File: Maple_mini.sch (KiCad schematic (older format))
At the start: 24 parts, among them P1 CONN_01X03, Q1 Q_NPN_BEC, Q2 Q_NPN_BEC, SW1 SW_PUSH, SW2 SW_PUSH, U1 STM32F103CBT6, X1 8.000Mhz

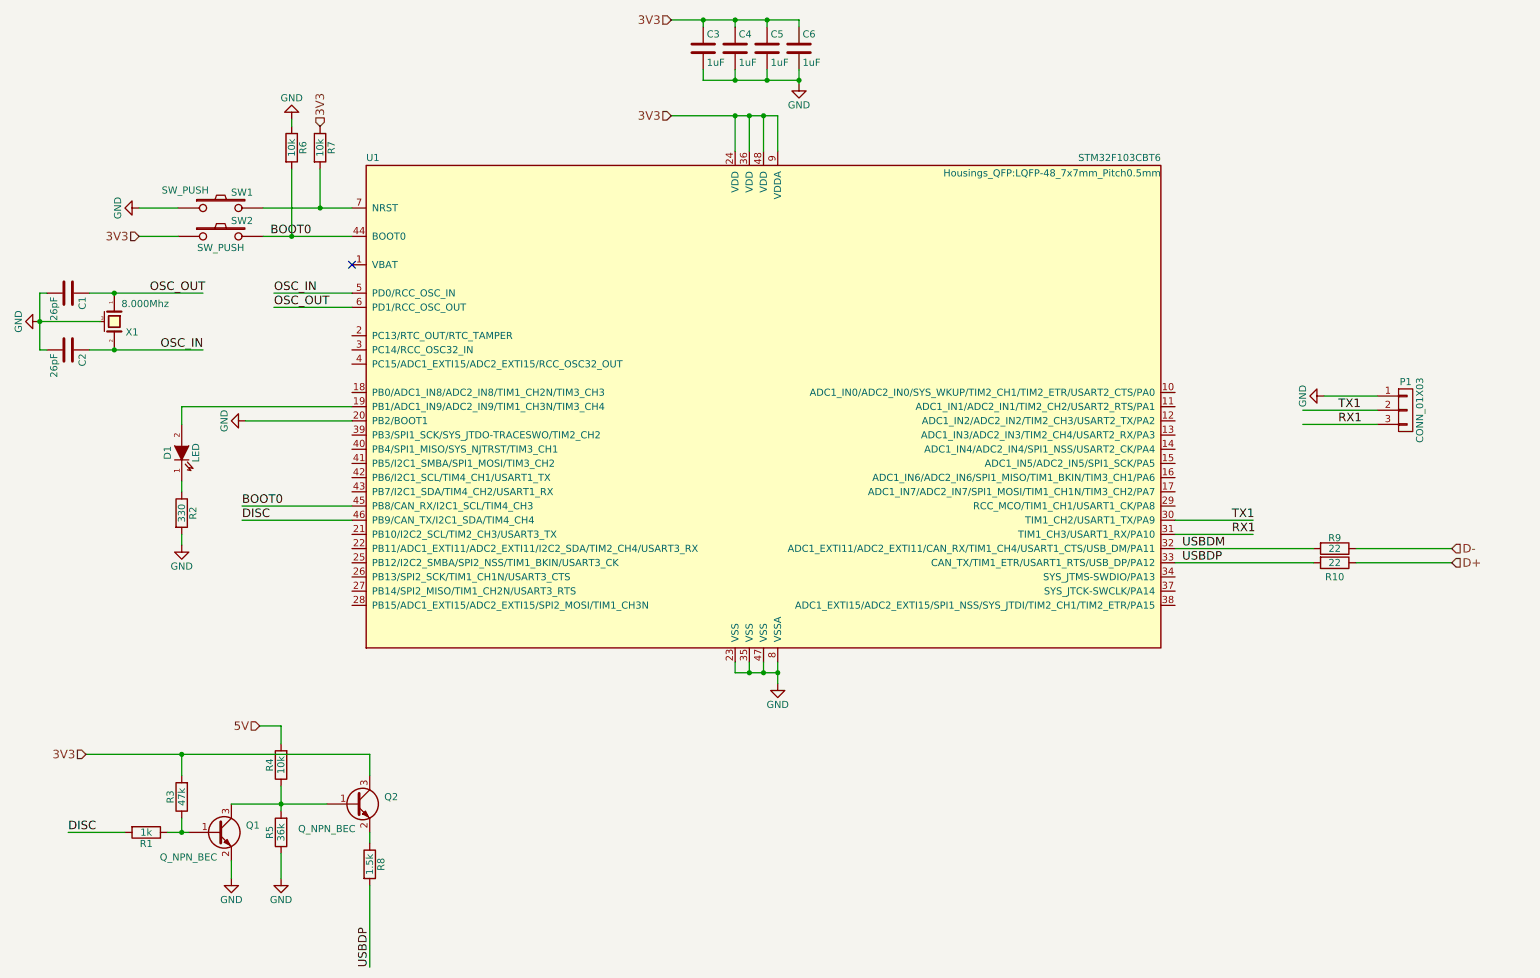
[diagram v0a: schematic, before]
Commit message: Change USB Disc circuit
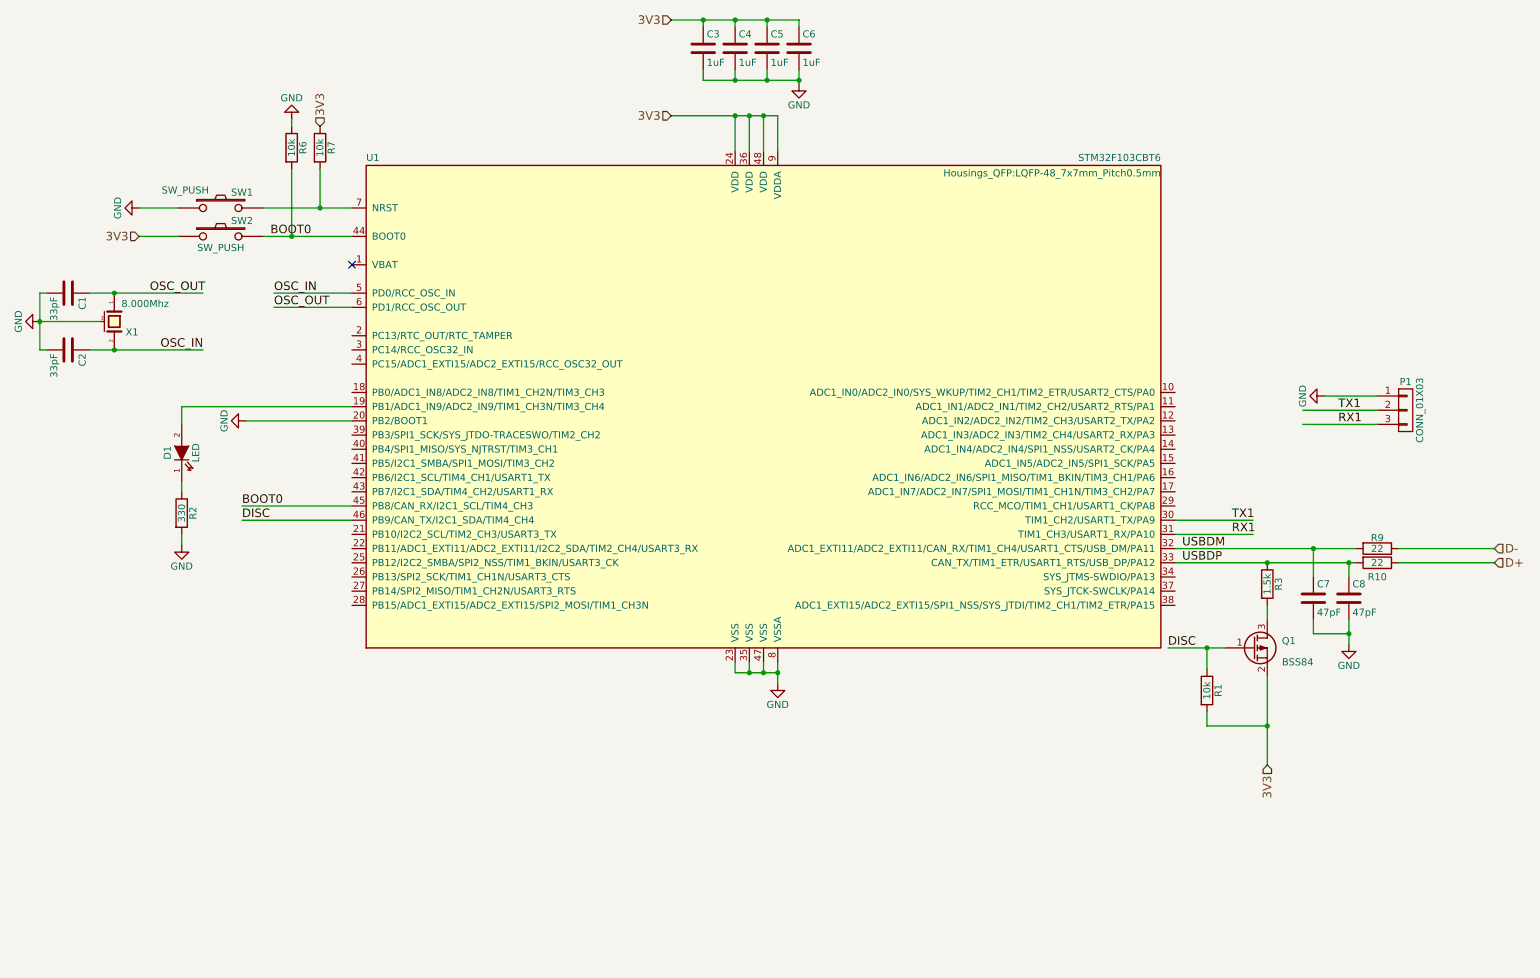
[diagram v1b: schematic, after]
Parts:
- removed Q1, Q2: Q_NPN_BEC, TO_SOT_Packages_SMD:SOT-23, symbol Q_NPN_BEC
- removed R4: 10k, Resistors_SMD:R_0603_HandSoldering, symbol R
- removed R5: 36k, Resistors_SMD:R_0603_HandSoldering, symbol R
- removed R8: 1.5k, Resistors_SMD:R_0603_HandSoldering, symbol R
- added C7, C8: 47pF, Capacitors_SMD:C_0603, symbol C
- added Q1: BSS84, TO_SOT_Packages_SMD:SOT-23, symbol Q_PMOS_GSD
- C1, C2: value 26pF -> 33pF
- R1: value 1k -> 10k; Part # 311-1.0KGRCT-ND -> (none); Unit price(won) 5.486 -> (none); Vender DigiKey -> (none)
- R3: value 47k -> 1.5k; Part # 311-47KGRCT-ND -> (none); Unit price(won) 11.36 -> (none); Vender DigiKey -> (none)
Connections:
- net labels removed: 5V
- wire segments 65 -> 62
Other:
- moved on the sheet: R10, R9
